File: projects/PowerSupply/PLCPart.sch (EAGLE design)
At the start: 31 parts, among them IC1 L7818CV, IC2 L7918CV, IC3 LM741P, IC4 LM741P, IC5 L7915CV, IC6 L7815CV, IC7 LM358N, IC8 LM358N, X1 MCU-PWR, X2 MCU-IN, X3 MCU-OUT

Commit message: feat: plc part modified
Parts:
- removed IC3, IC4: LM741P, linear:LM741P
- removed IC7, IC8: LM358N, linear:LM358N
- added R10: 10k, rcl:R-EU_0207/10
- added R11: 3.32k, rcl:R-EU_0207/10
- added R12, R9: 4.99k, rcl:R-EU_0207/10
- R1, R4: value 1k -> 10k
- R2: value 10k -> 3.32k
- R3, R6: value 10k -> 4.99k
- R5, R8: value 1k -> 3.32k
- X3: value MCU-OUT -> (none); device con-wago-508:W237-08P -> con-wago-508:W237-04P
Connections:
- removed net N$10: IC8B.OUT, X3-8.KL
- removed net N$5: R5.2, R6.1, X3-3.KL
- removed net N$6: IC3.OUT, R8.2, X3-4.KL
- removed net N$7: IC7A.OUT, X3-5.KL
- removed net N$8: IC7B.OUT, X3-6.KL
- removed net N$9: IC8A.OUT, X3-7.KL
- new net VCC: R11.2, R2.2, R5.2, R8.2
- net +15V: no longer IC7P.V+, IC8P.V+
- net +18V: no longer IC3.V+, IC4.V+
- net +5V: now also R7.1; no longer R5.1
- net -12V: now also R4.1; no longer R3.1
- net -15V: no longer IC7P.V-, IC8P.V-
- net -18V: no longer IC3.V-, IC4.V-
- net -5V: now also R10.1; no longer R7.1
- net GND: now also R12.2, R3.2, R9.2; no longer IC3.+IN, IC4.+IN, R2.2
- net N$1: now also R1.2, R2.1, R3.1, X3-1.KL; no longer IC4.-IN, R3.2, R4.1
- net N$2: now also R5.1, R6.1; no longer IC4.OUT
- net N$3: now also R9.1, X3-3.KL; no longer IC3.-IN
- net N$4: now also R10.2, R11.1, R12.1, X3-4.KL; no longer R1.2, R2.1, X3-1.KL
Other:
- moved on the sheet: R1, R2, R3, R4, R5, R6, R7, R8, X3-1, X3-2, X3-3, X3-4

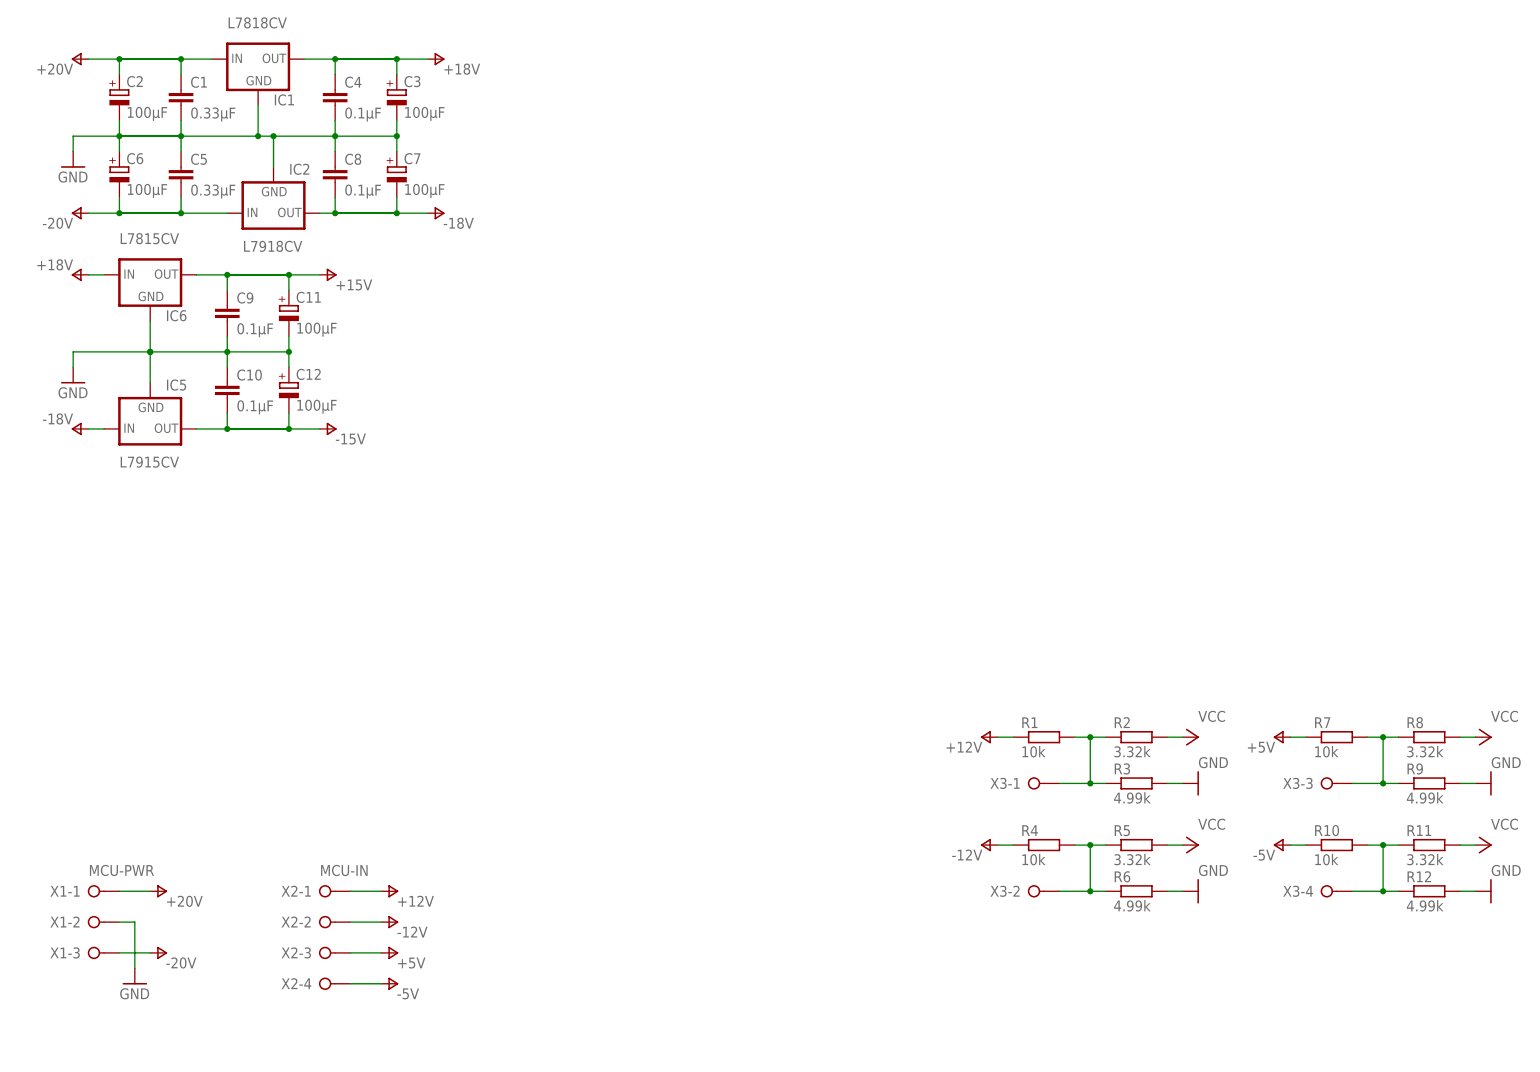
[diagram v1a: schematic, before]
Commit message: feat: plc part buck for vcc added
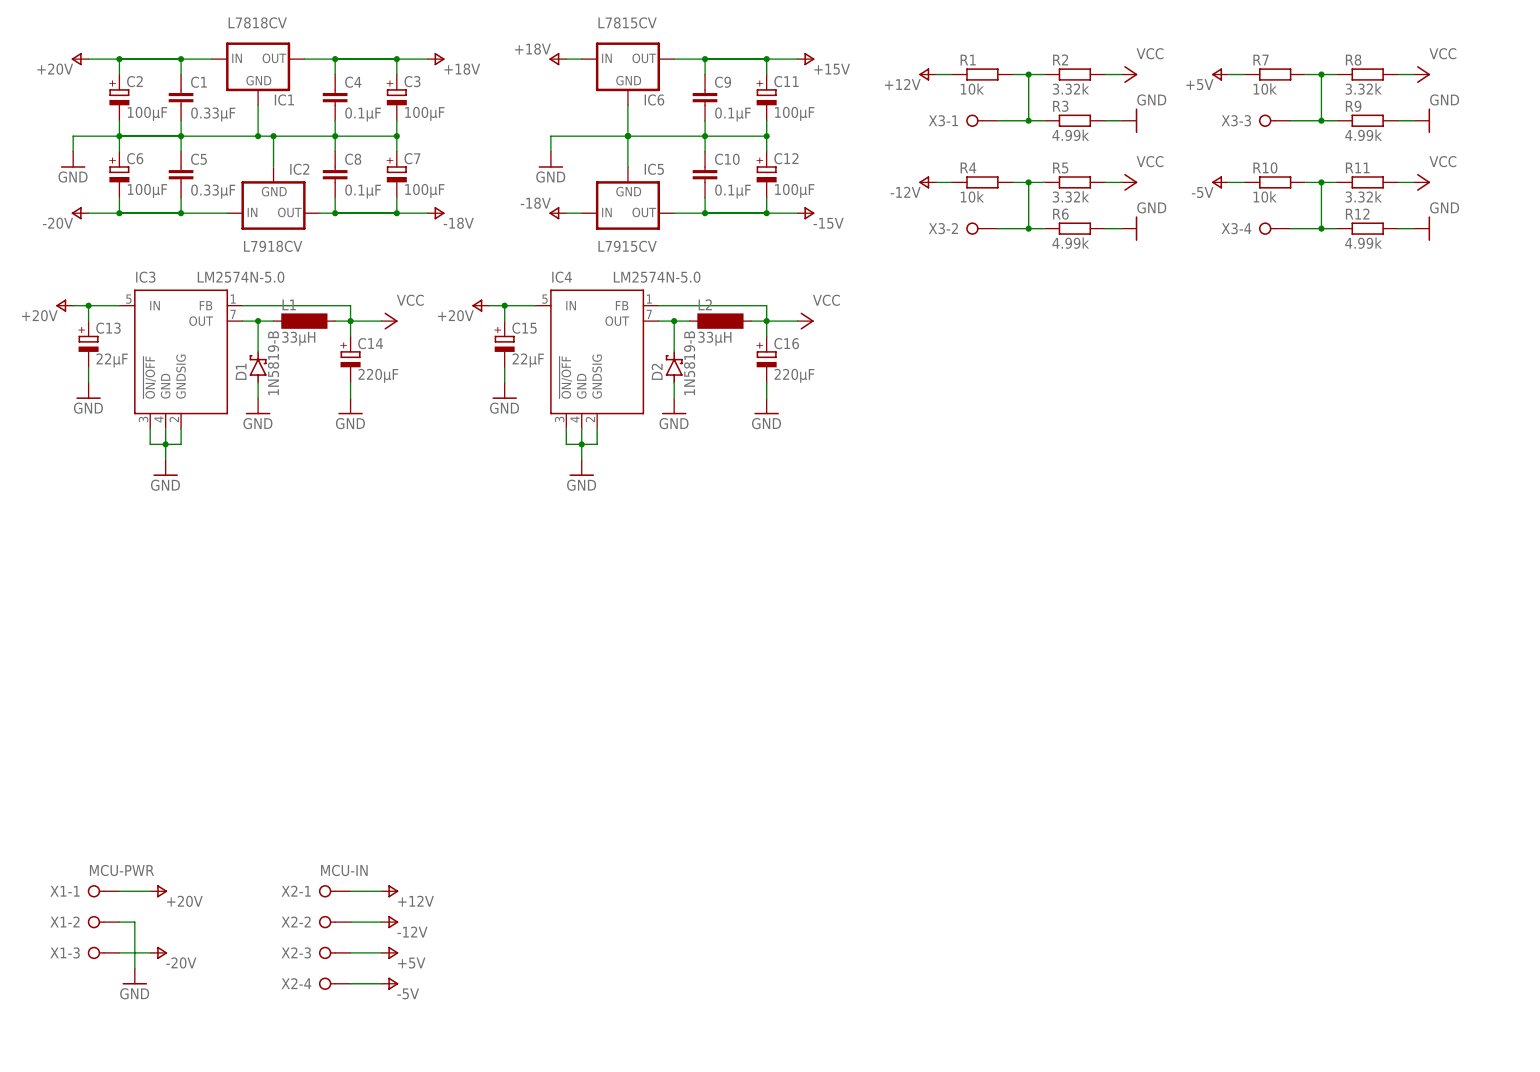
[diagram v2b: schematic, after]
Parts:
- added C13, C15: 22µF, rcl:CPOL-EUE2-5
- added C14, C16: 220µF, rcl:CPOL-EUE2-5
- added D1, D2: 1N5819-B, diode:1N5819-B
- added IC3, IC4: LM2574N-5.0, linear:LM2574N-5.0
- added L1, L2: 33µH, inductor-neosid:SD12-680
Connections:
- new net N$5: D1.C, IC3.OUT, L1.1
- new net N$6: D2.C, IC4.OUT, L2.1
- net +20V: now also C13.+, C15.+, IC3.IN, IC4.IN
- net GND: now also C13.-, C14.-, C15.-, C16.-, D1.A, D2.A, IC3.!ON/OFF, IC3.GND@PWR, IC3.GNDSIG, IC4.!ON/OFF, IC4.GND@PWR, IC4.GNDSIG
- net VCC: now also C14.+, C16.+, IC3.FB, IC4.FB, L1.2, L2.2
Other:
- moved on the sheet: C10, C11, C12, C9, IC5, IC6, R1, R10, R11, R12, R2, R3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

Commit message: feat: plc part modified and layout added
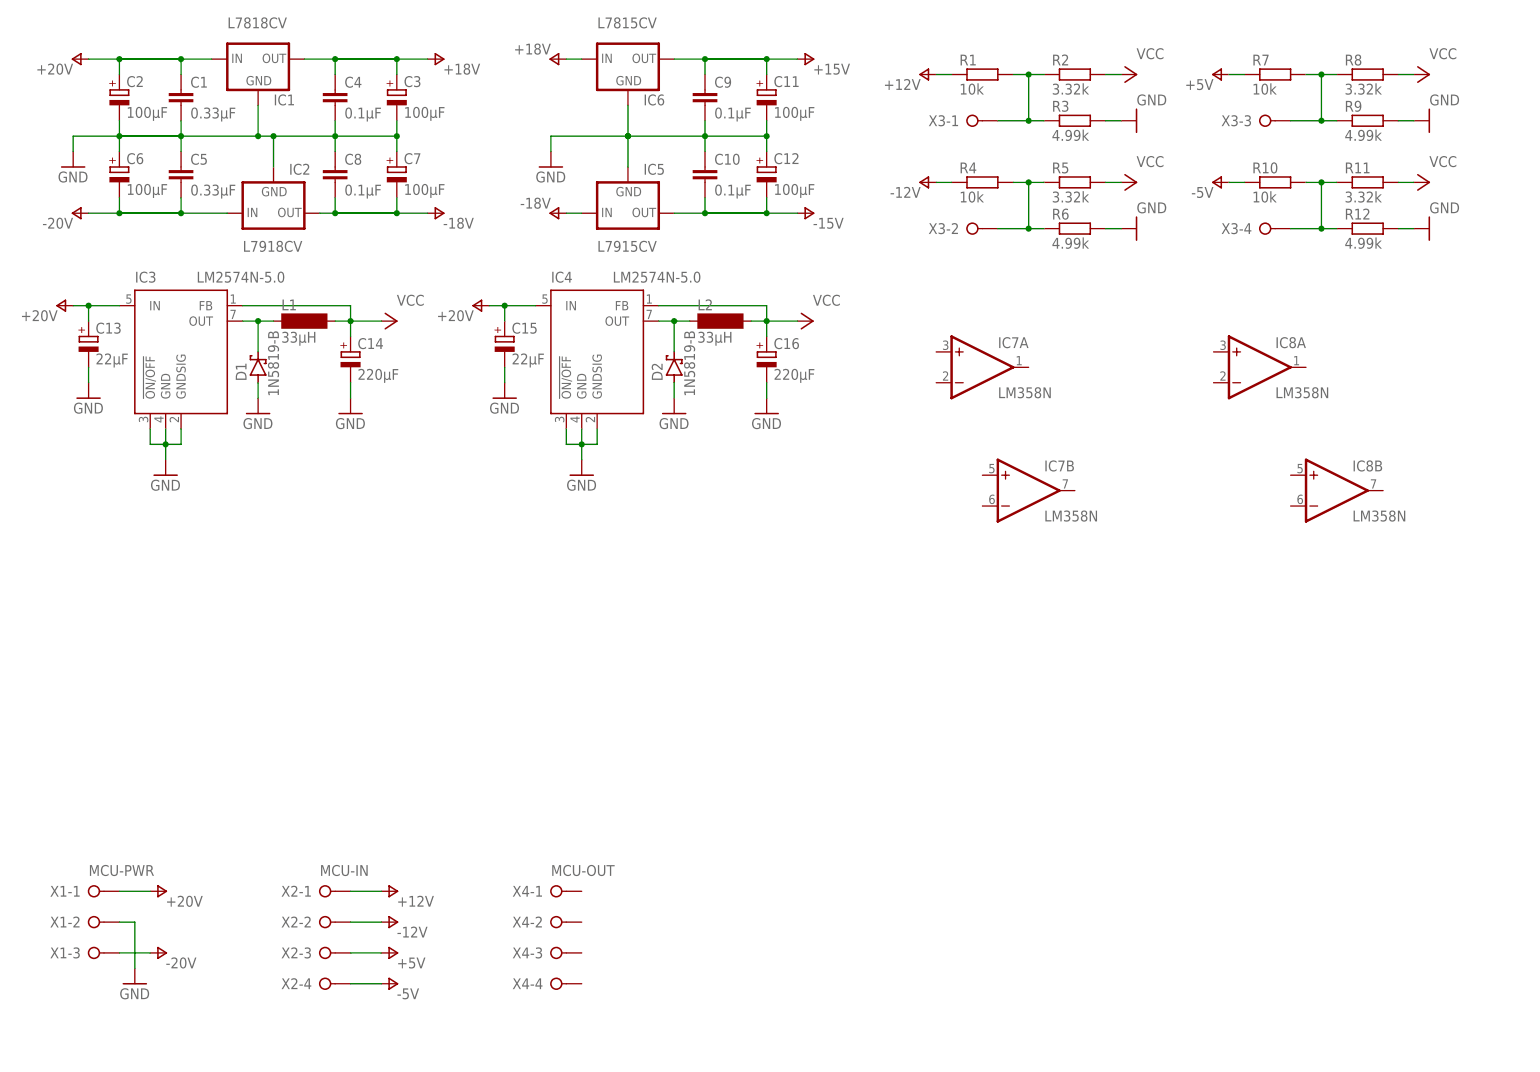
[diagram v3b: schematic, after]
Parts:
- added IC7, IC8: LM358N, linear:LM358N
- added X4: MCU-OUT, con-wago-508:W237-04P
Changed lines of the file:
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@@
 <part name="GND14" library="supply1" library_urn="urn:adsk.eagle:library:371" deviceset="GND" device=""/>
 <part name="GND15" library="supply1" library_urn="urn:adsk.eagle:library:371" deviceset="GND" device=""/>
+<part name="IC7" library="linear" library_urn="urn:adsk.eagle:library:262" deviceset="LM358" device="N" package3d_urn="urn:adsk.eagle:package:16409/2"/>
+<part name="IC8" library="linear" library_urn="urn:adsk.eagle:library:262" deviceset="LM358" device="N" package3d_urn="urn:adsk.eagle:package:16409/2"/>
+<part name="X4" library="con-wago-508" library_urn="urn:adsk.eagle:library:196" deviceset="W237-04P" device="" package3d_urn="urn:adsk.eagle:package:10735/1" value="MCU-OUT"/>
 </parts>
 <sheets>
@@
 <attribute name="VALUE" x="127" y="106.68" size="1.778" layer="96"/>
 </instance>
+<instance part="IC7" gate="A" x="165.1" y="116.84" smashed="yes">
+<attribute name="NAME" x="167.64" y="120.015" size="1.778" layer="95"/>
+<attribute name="VALUE" x="167.64" y="111.76" size="1.778" layer="96"/>
+</instance>
+<instance part="IC7" gate="B" x="172.72" y="96.52" smashed="yes">
+<attribute name="NAME" x="175.26" y="99.695" size="1.778" layer="95"/>
+<attribute name="VALUE" x="175.26" y="91.44" size="1.778" layer="96"/>
+</instance>
+<instance part="IC8" gate="A" x="210.82" y="116.84" smashed="yes">
+<attribute name="NAME" x="213.36" y="120.015" size="1.778" layer="95"/>
+<attribute name="VALUE" x="213.36" y="111.76" size="1.778" layer="96"/>
+</instance>
+<instance part="IC8" gate="B" x="223.52" y="96.52" smashed="yes">
+<attribute name="NAME" x="226.06" y="99.695" size="1.778" layer="95"/>
+<attribute name="VALUE" x="226.06" y="91.44" size="1.778" layer="96"/>
+</instance>
+<instance part="X4" gate="-1" x="93.98" y="30.48" smashed="yes">
+<attribute name="NAME" x="92.71" y="31.369" size="1.778" layer="95" rot="R180"/>
+</instance>
+<instance part="X4" gate="-2" x="93.98" y="25.4" smashed="yes">
+<attribute name="NAME" x="92.71" y="26.289" size="1.778" layer="95" rot="R180"/>
+</instance>
+<instance part="X4" gate="-3" x="93.98" y="20.32" smashed="yes">
+<attribute name="NAME" x="92.71" y="21.209" size="1.778" layer="95" rot="R180"/>
+</instance>
+<instance part="X4" gate="-4" x="93.98" y="15.24" smashed="yes">
+<attribute name="VALUE" x="93.98" y="33.02" size="1.778" layer="96"/>
+<attribute name="NAME" x="92.71" y="16.129" size="1.778" layer="95" rot="R180"/>
+</instance>
 </instances>

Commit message: feat: plc part modified
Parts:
- C14, C16: value 220µF -> 470µF
- L1, L2: value 33µH -> 68µH; device inductor-neosid:SD12-680 -> inductor-neosid:SD12K100
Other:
- moved on the sheet: C14, C16, D1, D2, L1, L2

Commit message: feat: plca part modified
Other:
- moved on the sheet: C13, C15
